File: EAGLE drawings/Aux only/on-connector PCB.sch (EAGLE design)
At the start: 19 parts, among them IC1 TINY13-20MM0

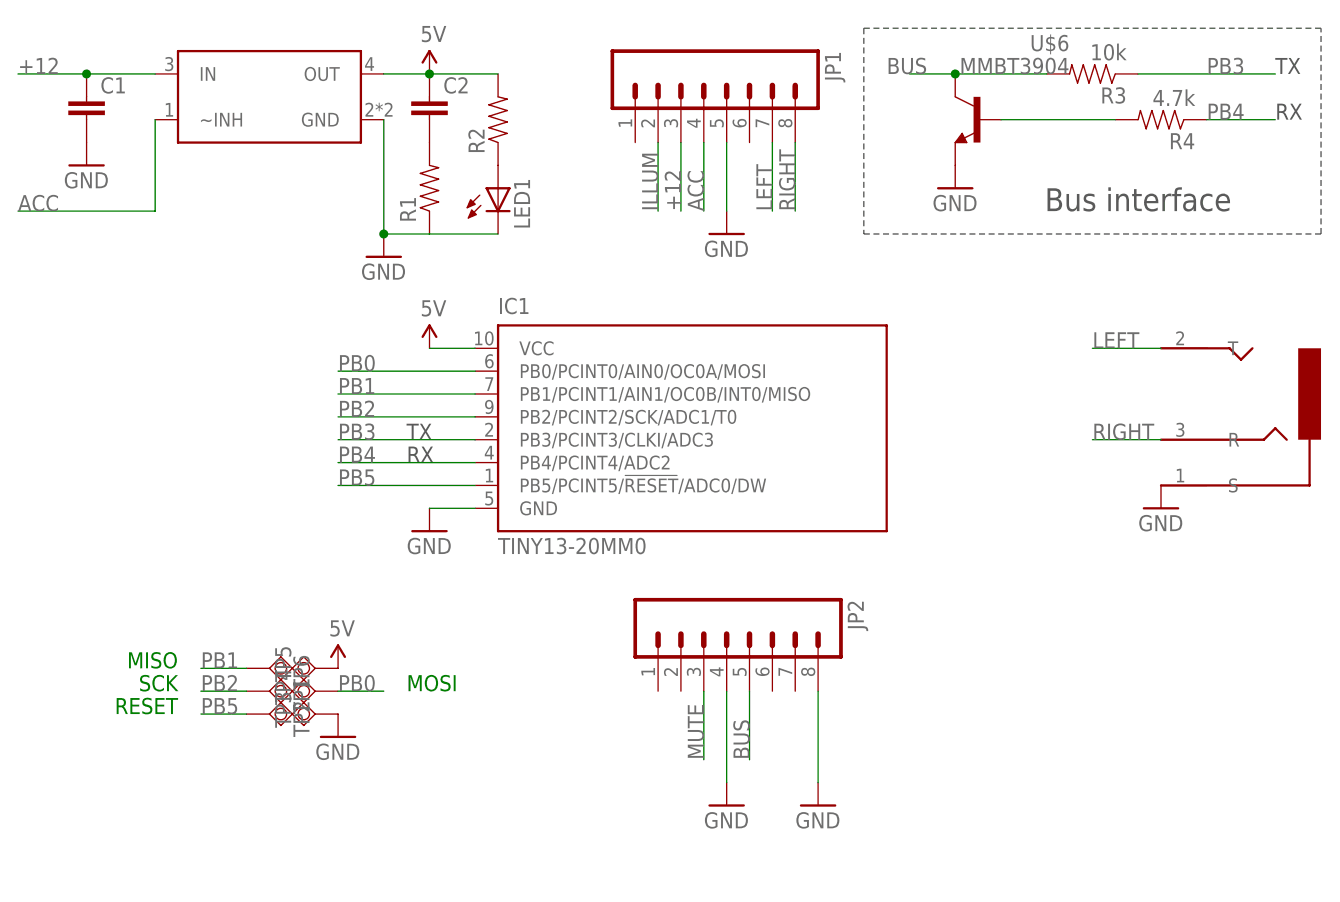
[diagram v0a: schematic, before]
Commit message: Updated aux-only board, preparing to switch to 32/16/8U2
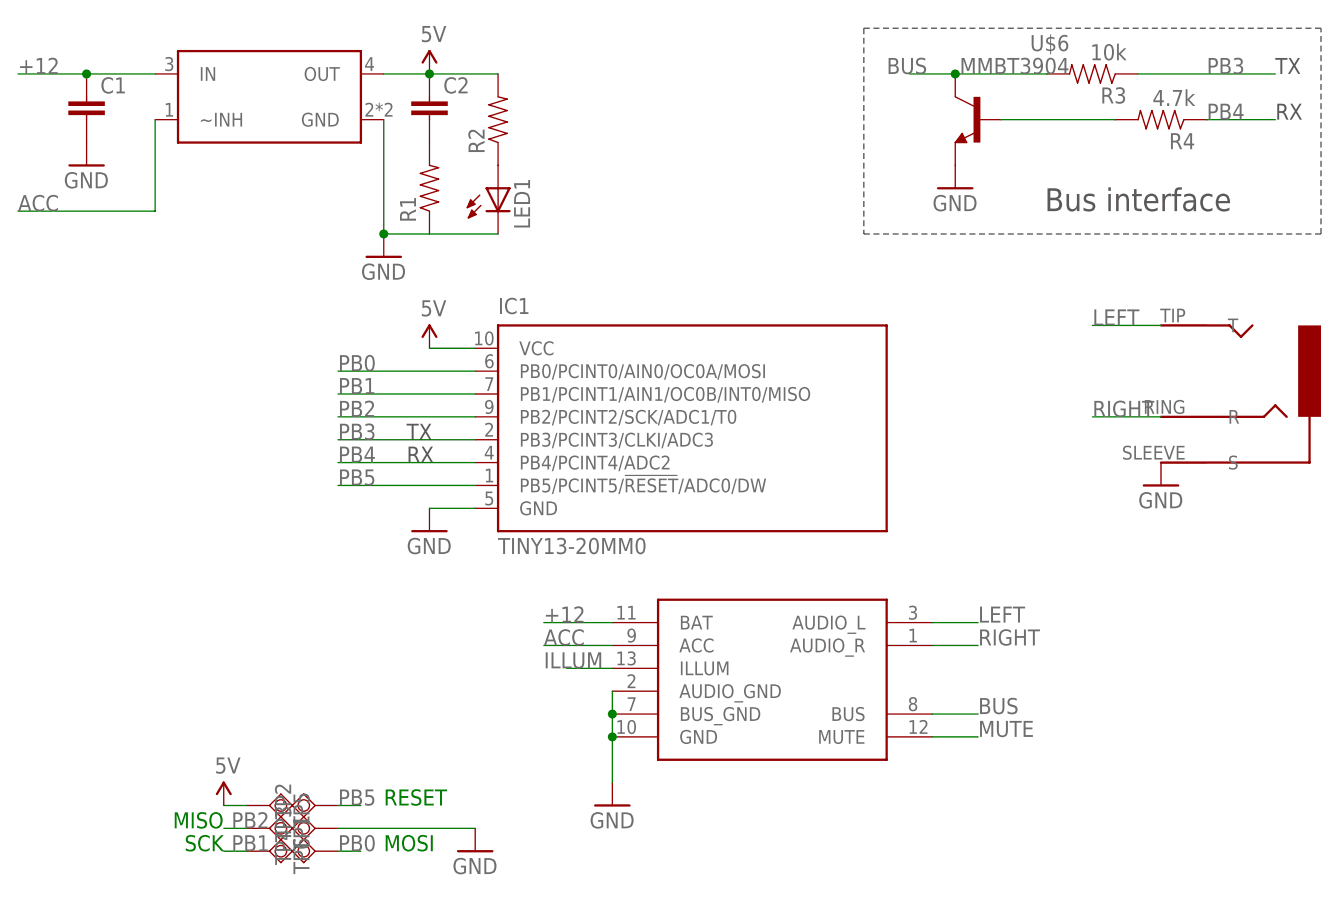
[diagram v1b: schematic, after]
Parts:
- removed JP1, JP2: (no value), SparkFun:M081X08
- added U$1: PANASONIC_CN702_BACKBOARD, personal:PANASONIC_CN702_BACKBOARD
- TP1, TP2, TP3, TP4: value TPSQTP06R -> TPSQTP07R; device testpad:TPSQTP06R -> testpad:TPSQTP07R
- TP5: value TPSQTP06R -> TPSQTP07SQ; device testpad:TPSQTP06R -> testpad:TPSQTP07SQ
- TP6: value TPSQTP06SQ -> TPSQTP07R; device testpad:TPSQTP06SQ -> testpad:TPSQTP07R
- U$2: value STEREO_JACK_SJ1-353XNG3NG -> STEREO_JACK_SJ_352X; device personal:STEREO_JACK_SJ1-353XNG3NG -> personal:STEREO_JACK_SJ_352X
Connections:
- net +12: now also U$1.BAT; no longer JP1.3
- net ACC: now also U$1.ACC; no longer JP1.4
- net BUS: now also U$1.BUS; no longer JP2.5
- net GND: now also U$1.AUDIO_GND, U$1.BUS_GND, U$1.GND; no longer JP1.5, JP2.4, JP2.8
- net ILLUM: now also U$1.ILLUM; no longer JP1.2
- net LEFT: now also U$1.AUDIO_L; no longer JP1.7
- net MUTE: now also U$1.MUTE; no longer JP2.3
- net RIGHT: now also U$1.AUDIO_R; no longer JP1.8
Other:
- moved on the sheet: TP1, TP2, TP3, TP4, TP5, TP6
